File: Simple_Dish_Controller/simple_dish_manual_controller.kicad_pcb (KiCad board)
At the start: 2 copper layers, 13 parts, among them J1 Screw_Terminal_01x02, J2 DA15_Socket, J3 DA15_Socket, Q1 PZT2222A, Q2 PZT2222A, Q3 PZT2222A, Q4 PZT2222A, U1 AMS1117-5.0, U4 ICM7555xP, U5 ICM7555xP

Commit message: 777 chip is now SMD
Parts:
- added J4: CRJ022-G-TH, 2-port JR45:CUI_CRJ022-G-TH, F.Cu at (97.5, 78.1)
- added J5: CRJ022-G-TH, 2-port JR45:CUI_CRJ022-G-TH, F.Cu at (50.2, 78.1)
- C1, C2: footprint GRM219R61C226ME15K:CAPC2012X100N -> Cap_SMD_22uF_0805:CAPC2012X100N
- J2, J3: value DA15_Socket -> 1-Pin Terminal Block; footprint Connector_Dsub:DSUB-15_Socket_Horizontal_P2.77x2.54mm_EdgePinOffset9.40mm -> 2-port JR45:CUI_CRJ022-G-TH
- U4: value ICM7555xP -> NE555PS; footprint Package_SO:SOIC-8_3.9x4.9mm_P1.27mm -> NE555P Osc Chip SMD:SOIC127P780X200-8N
- U5: value ICM7555xP -> NE555PS; footprint Package_DIP:DIP-8_W7.62mm -> NE555P Osc Chip SMD:SOIC127P780X200-8N
- moved C1 339.8 mm to (89.9, 93.3)
- moved U1 317.6 mm to (85.0, 104.5)
- moved C2 314.9 mm to (89.9, 96.3)
- moved J3 313.8 mm to (50.2, 54.3)
- moved R1 304.1 mm to (88.9, 98.7)
- moved J1 298.6 mm to (82.6, 95.9)
- moved U5 279.8 mm to (72.8, 62.8)
- moved Q3 277.8 mm to (72.5, 46.4)
- moved Q4 266.3 mm to (72.5, 54.7)
- moved J2 258.1 mm to (97.5, 54.3)
- moved U4 240.2 mm to (120.1, 62.8)
- moved Q2 214.8 mm to (119.8, 54.7)
- moved Q1 196.2 mm to (119.8, 46.4)
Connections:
- net Net-(Q4-B) renamed /Azimuth/Pul sig
- net Net-(U4-R) renamed /Elevation/Pulse Enable
- net Net-(U5-R) renamed /Azimuth/Pulse Enable
- Q1 pad 2: /Elevation/Pul -> /Elevation/Dir
- Q2 pad 1: Net-(Q2-B) -> /Elevation/Pul sig
- Q2 pad 2: /Elevation/Dir -> /Elevation/Pul
- U4 pad 3: Net-(Q1-B) -> /Elevation/Pul sig

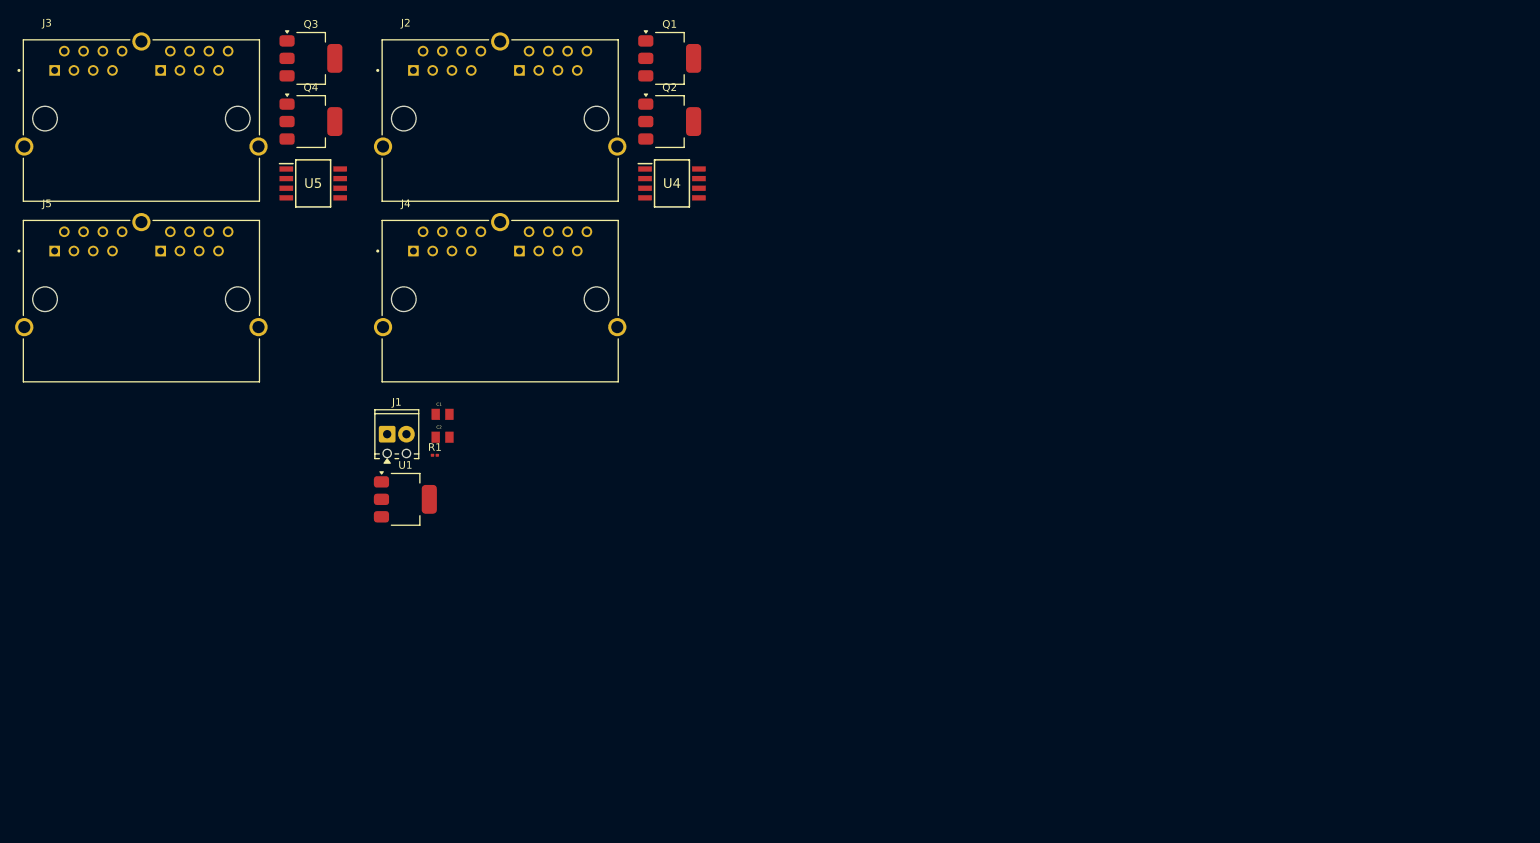
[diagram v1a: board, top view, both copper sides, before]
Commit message: Added parts dir
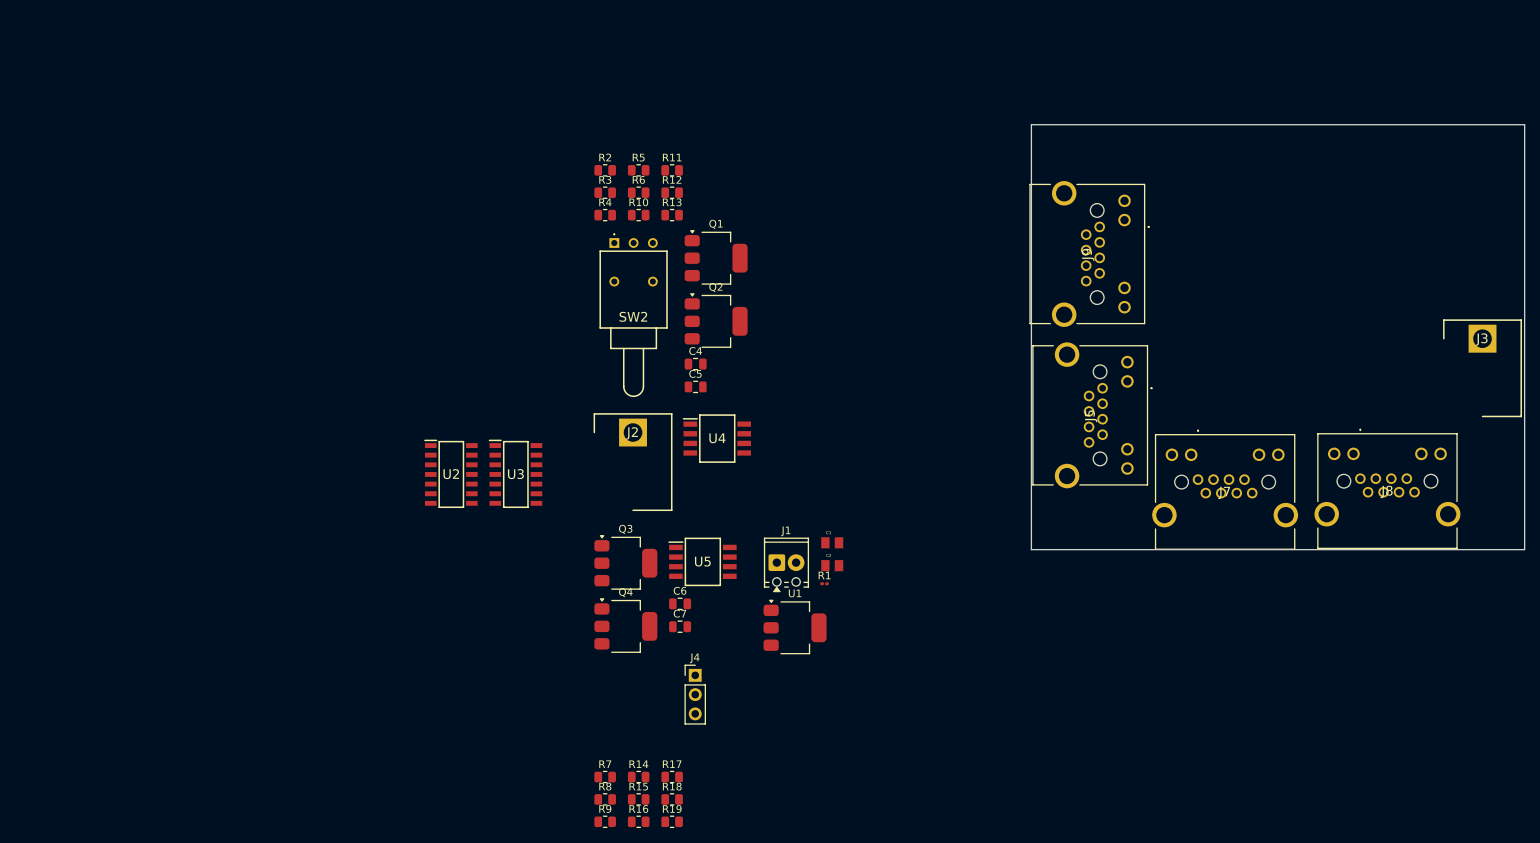
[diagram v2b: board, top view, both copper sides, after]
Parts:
- added C4: 10nF, Capacitor_SMD:C_0805_2012Metric, F.Cu at (123.2, 86.6)
- added C5: 100nF, Capacitor_SMD:C_0805_2012Metric, F.Cu at (123.2, 89.7)
- added C6: 10nF, Capacitor_SMD:C_0805_2012Metric, F.Cu at (121.2, 118.2)
- added C7: 100nF, Capacitor_SMD:C_0805_2012Metric, F.Cu at (121.2, 121.3)
- added J7: RJ45 port shielded, RA, TH, DishController_footprints:RJ45 Port Shielded, Right Angle TH, F.Cu at (189.5, 101.9)
- added J8: RJ45 port shielded, RA, TH, DishController_footprints:RJ45 Port Shielded, Right Angle TH, F.Cu at (210.8, 101.8)
- added J9: RJ45 port shielded, RA, TH, DishController_footprints:RJ45 Port Shielded, Right Angle TH, F.Cu at (176.5, 68.6)
- added R10: 10k, Resistor_SMD:R_0805_2012Metric, F.Cu at (115.7, 67.0)
- added R11: 10k, Resistor_SMD:R_0805_2012Metric, F.Cu at (120.2, 61.1)
- added R12: 10k, Resistor_SMD:R_0805_2012Metric, F.Cu at (120.2, 64.1)
- added R13: 10k, Resistor_SMD:R_0805_2012Metric, F.Cu at (120.2, 67.0)
- added R14: 10k, Resistor_SMD:R_0805_2012Metric, F.Cu at (115.7, 141.1)
- added R15: 10k, Resistor_SMD:R_0805_2012Metric, F.Cu at (115.7, 144.0)
- added R16: 10k, Resistor_SMD:R_0805_2012Metric, F.Cu at (115.7, 147.0)
- added R17: 10k, Resistor_SMD:R_0805_2012Metric, F.Cu at (120.2, 141.1)
- added R18: 820, Resistor_SMD:R_0805_2012Metric, F.Cu at (120.2, 144.0)
- added R19: 6.8k, Resistor_SMD:R_0805_2012Metric, F.Cu at (120.2, 147.0)
- added R2: 820, Resistor_SMD:R_0805_2012Metric, F.Cu at (111.3, 61.1)
- added R3: 10k, Resistor_SMD:R_0805_2012Metric, F.Cu at (111.3, 64.1)
- added R4: 6.8k, Resistor_SMD:R_0805_2012Metric, F.Cu at (111.3, 67.0)
- added R5: 10k, Resistor_SMD:R_0805_2012Metric, F.Cu at (115.7, 61.1)
- added R6: 1k, Resistor_SMD:R_0805_2012Metric, F.Cu at (115.7, 64.1)
- added R7: 10k, Resistor_SMD:R_0805_2012Metric, F.Cu at (111.3, 141.1)
- added R8: 10k, Resistor_SMD:R_0805_2012Metric, F.Cu at (111.3, 144.0)
- added R9: 1k, Resistor_SMD:R_0805_2012Metric, F.Cu at (111.3, 147.0)
- added SW2: SW_SPDT_312, SPDT-90-Deg-On-Off-On:B18JH, F.Cu at (112.5, 70.7)
- added U2: 74LS08, 74LS08_SOIC:SOIC127P600X175-14N, F.Cu at (91.1, 101.2)
- added U3: 74LS32, 74LS32_SOIC:SOIC127P600X175-14N, F.Cu at (99.6, 101.2)
- J2, J3: footprint 2-port JR45:CUI_CRJ022-G-TH -> 1-Pin Barrier Terminal Block:RHDR1W160P0X826_1X1_1020X1270X1270P
- J4: value CRJ022-G-TH -> Conn_01x03_Pin; footprint 2-port JR45:CUI_CRJ022-G-TH -> Connector_PinHeader_2.54mm:PinHeader_1x03_P2.54mm_Vertical
- J5: value CRJ022-G-TH -> RJ45 port shielded, RA, TH; footprint 2-port JR45:CUI_CRJ022-G-TH -> DishController_footprints:RJ45 Port Shielded, Right Angle TH
- moved J3 179.1 mm to (226.9, 83.3)
- moved J5 127.2 mm to (176.9, 89.8), turned to -90 degrees
- moved Q3 78.4 mm to (114.0, 112.9)
- moved Q4 78.4 mm to (114.0, 121.2)
- moved U5 71.6 mm to (124.2, 112.7)
- moved J4 55.8 mm to (123.2, 127.7)
- moved R1 54.1 mm to (140.2, 115.6)
- moved C1 54.1 mm to (141.2, 110.2)
- moved C2 54.1 mm to (141.2, 113.2)
- moved J1 54.1 mm to (133.9, 112.8)
- moved U1 54.1 mm to (136.3, 121.4)
- moved J2 44.9 mm to (115.0, 95.7)
- moved U4 34.2 mm to (126.1, 96.5)
- moved Q1 27.0 mm to (126.0, 72.7)
- moved Q2 27.0 mm to (126.0, 81.0)
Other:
- board outline added: 65 x 56 mm

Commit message: Latest update
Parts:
- removed C1, C2: 22uF, Cap_SMD_22uF_0805:CAPC2012X100N
- removed C5: 100nF, Capacitor_SMD:C_0805_2012Metric
- removed J7, J8, J9: RJ45 port shielded, RA, TH, DishController_footprints:RJ45 Port Shielded, Right Angle TH
- removed Q2: PZT2222A, Package_TO_SOT_SMD:SOT-223-3_TabPin2
- removed R2: 820, Resistor_SMD:R_0805_2012Metric
- removed R4: 6.8k, Resistor_SMD:R_0805_2012Metric
- removed SW2: SW_SPDT_312, SPDT-90-Deg-On-Off-On:B18JH
- added C3: 100nF, DishFootprints:C_0805, F.Cu at (107.6, 85.9)
- added J10: Screw Terminal 4 pins to board, DishFootprintsSupplier:TERM_SCREW_01x04_VERTICAL_KEYSTONE_7690, F.Cu at (185.5, 104.5)
- added J6: Conn_01x03_Pin, DishFootprints:PinHeader_1x03_P2.54mm_Vertical, F.Cu at (169.8, 76.1)
- added Q5: PZT2222A, DishFootprints:SOT-223, F.Cu at (124.3, 90.4)
- added R20: 820, DishFootprints:R_0805, F.Cu at (140.3, 82.3)
- added R21: 6.8k, DishFootprints:R_0805, F.Cu at (140.3, 85.2)
- C4: value 10nF -> 100nF; footprint Capacitor_SMD:C_0805_2012Metric -> DishFootprints:C_0805
- C6: value 10nF -> 10uF; footprint Capacitor_SMD:C_0805_2012Metric -> DishFootprints:C_0805
- C7: value 100nF -> 10uF; footprint Capacitor_SMD:C_0805_2012Metric -> DishFootprints:C_0805
- J1: footprint TerminalBlock_Phoenix:TerminalBlock_Phoenix_MPT-0,5-2-2.54_1x02_P2.54mm_Horizontal -> DishFootprints:TerminalBlock_Phoenix_MKDS-1,5-2-5.08_1x02_P5.08mm_Horizontal
- J2: value 1-Pin Terminal Block -> Conn_01x02_Pin; footprint 1-Pin Barrier Terminal Block:RHDR1W160P0X826_1X1_1020X1270X1270P -> DishFootprints:PinHeader_1x02_P2.54mm_Vertical
- J3: value 1-Pin Terminal Block -> DE-15_VGA_FEMALE_CONN; footprint 1-Pin Barrier Terminal Block:RHDR1W160P0X826_1X1_1020X1270X1270P -> DishFootprintsSupplier:DB15_VGA_FEMALE_CONN
- J4: footprint Connector_PinHeader_2.54mm:PinHeader_1x03_P2.54mm_Vertical -> DishFootprints:PinHeader_1x03_P2.54mm_Vertical
- J5: value RJ45 port shielded, RA, TH -> DE-15_VGA_FEMALE_CONN; footprint DishController_footprints:RJ45 Port Shielded, Right Angle TH -> DishFootprintsSupplier:DB15_VGA_FEMALE_CONN
- Q1, Q3, Q4: footprint Package_TO_SOT_SMD:SOT-223-3_TabPin2 -> DishFootprints:SOT-223
- R1: footprint Resistor_SMD:R_0201_0603Metric -> DishFootprints:R_0805
- R13, R18, R19: footprint Resistor_SMD:R_0805_2012Metric -> DishFootprints:R_0805
- U1: footprint Package_TO_SOT_SMD:SOT-223-3_TabPin2 -> DishFootprints:SOT-223-3_TabPin2
- U2: footprint 74LS08_SOIC:SOIC127P600X175-14N -> DishFootprints:SOIC-14_3.9x8.7mm_P1.27mm
- U3: footprint 74LS32_SOIC:SOIC127P600X175-14N -> DishFootprints:SOIC-14_3.9x8.7mm_P1.27mm
- U4, U5: value NE555PS -> NE555D; footprint NE555P Osc Chip SMD:SOIC127P780X200-8N -> DishFootprints:SOIC-8_3.9x4.9mm_P1.27mm
- moved U3 104.2 mm to (203.1, 88.7)
- moved U2 95.4 mm to (185.5, 87.6)
- moved U4 85.4 mm to (211.3, 90.3)
- moved Q1 82.6 mm to (208.5, 74.5)
- moved J4 66.8 mm to (169.7, 79.7), turned to 90 degrees
- moved R17 65.4 mm to (98.5, 79.3)
- moved R19 65.4 mm to (98.5, 85.2)
- moved R7 65.4 mm to (89.7, 79.3)
- moved R9 65.4 mm to (89.7, 85.2)
- moved R14 65.4 mm to (94.1, 79.3)
- moved R16 65.4 mm to (94.1, 85.2)
- moved R18 65.4 mm to (98.5, 82.3)
- moved R8 65.4 mm to (89.7, 82.3)
- moved R15 65.4 mm to (94.1, 82.3)
- moved J2 56.1 mm to (169.7, 83.2), turned to 90 degrees
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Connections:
- C4 pad 1: Net-(U4-CONT) -> Net-(U4-THR)
- C7 pad 1: Net-(U5-THRES) -> Net-(U4-CV)
- J2 pad 1: Shield -> /IN_5VDC_SWITCH
- J3 pad 1: Shield -> +5V
- J5 pad 11: unconnected-(J5-A/K_3-Pad11) -> /Elevation/Pul
- J5 pad 12: unconnected-(J5-A/K_4-Pad12) -> /Elevation/Dir
- J5 pad 3: /Azimuth/Limit Sw1 -> /Elevation/Limit Sw1
- J5 pad 4: /Azimuth/Limit Sw2 -> /Elevation/Limit Sw2
- Q1 pad 1: Net-(Q1-B) -> /Elevation/Pul sig
- Q1 pad 2: /Elevation/Dir -> /Elevation/Pul
- R18 pad 2: Net-(U5-DISCH) -> Net-(U5-DIS)
- R19 pad 1: Net-(U5-THRES) -> Net-(U5-DIS)
- R19 pad 2: Net-(U5-DISCH) -> Net-(U5-THR)
- R6 pad 2: Net-(Q1-B) -> Net-(Q5-B)
- U4 pad 2: Net-(U4-THRES) -> Net-(U4-THR)
- U4 pad 5: Net-(U4-CONT) -> Net-(U4-CV)
- U4 pad 6: Net-(U4-THRES) -> Net-(U4-THR)
- U5 pad 2: Net-(U5-THRES) -> Net-(U5-THR)
- U5 pad 6: Net-(U5-THRES) -> Net-(U5-THR)
- U5 pad 7: Net-(U5-DISCH) -> Net-(U5-DIS)

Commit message: Updates
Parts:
- removed J10: Screw Terminal 4 pins to board, DishFootprintsSupplier:TERM_SCREW_01x04_VERTICAL_KEYSTONE_7690
- removed Q5: PZT2222A, DishFootprints:SOT-223
- removed R20: 820, DishFootprints:R_0805
- removed R21: 6.8k, DishFootprints:R_0805
- added C1: 22uF, Capacitor_SMD:C_1206_3216Metric, F.Cu at (127.6, 72.3)
- added C10: 10uF, Capacitor_SMD:C_1206_3216Metric, F.Cu at (138.2, 132.5)
- added C2: 22uF, Capacitor_SMD:C_1206_3216Metric, F.Cu at (127.6, 75.7)
- added C5: 0.1uF, Capacitor_SMD:C_1206_3216Metric, F.Cu at (250.3, 78.2)
- added C8: 0.1uF, Capacitor_SMD:C_1206_3216Metric, F.Cu at (138.2, 125.8)
- added C9: 100nF, Capacitor_SMD:C_1206_3216Metric, F.Cu at (138.2, 129.1)
- added D1: LED, LED_SMD:LED_1206_3216Metric, F.Cu at (137.8, 84.4)
- added J7: Azimuth DE-15, DishFootprints:DE15_VGA_FEMALE_CONN, F.Cu at (187.4, 110.4)
- added Q2: MMBT2222A, Package_TO_SOT_SMD:SOT-23, F.Cu at (260.2, 83.5)
- added R2: 820, Resistor_SMD:R_1206_3216Metric, F.Cu at (244.7, 53.9)
- added R4: 10k, Resistor_SMD:R_1206_3216Metric, F.Cu at (244.7, 60.6)
- added REF**: Raspberry_Pi_HAT_Side_DE15_Outline, DishFootprints:Raspberry_Pi_HAT_Side_DE15_Outline, F.Cu at (170.8, 50.1)
- C3, C4: value 100nF -> 0.1uF; footprint DishFootprints:C_0805 -> Capacitor_SMD:C_1206_3216Metric
- C6: value 10uF -> 100nF; footprint DishFootprints:C_0805 -> Capacitor_SMD:C_1206_3216Metric
- C7: footprint DishFootprints:C_0805 -> Capacitor_SMD:C_1206_3216Metric
- J1: footprint DishFootprints:TerminalBlock_Phoenix_MKDS-1,5-2-5.08_1x02_P5.08mm_Horizontal -> TerminalBlock_Phoenix:TerminalBlock_Phoenix_MKDS-1,5-2-5.08_1x02_P5.08mm_Horizontal
- J2: footprint DishFootprints:PinHeader_1x02_P2.54mm_Vertical -> Connector_PinHeader_2.54mm:PinHeader_1x02_P2.54mm_Vertical
- J3: value DE-15_VGA_FEMALE_CONN -> Screw Terminal To Chassis; footprint DishFootprintsSupplier:DB15_VGA_FEMALE_CONN -> DishFootprints:TERM_SCREW_01x04_VERTICAL_KEYSTONE_7690
- J4, J6: footprint DishFootprints:PinHeader_1x03_P2.54mm_Vertical -> Connector_PinHeader_2.54mm:PinHeader_1x03_P2.54mm_Vertical
- J5: value DE-15_VGA_FEMALE_CONN -> Elevation DE-15; footprint DishFootprintsSupplier:DB15_VGA_FEMALE_CONN -> DishFootprints:DE15_VGA_FEMALE_CONN
- Q1, Q3, Q4: value PZT2222A -> MMBT2222A; footprint DishFootprints:SOT-223 -> Package_TO_SOT_SMD:SOT-23
- R1: value 1k5 -> 1k; footprint DishFootprints:R_0805 -> Resistor_SMD:R_0805_2012Metric
- R10: value 10k -> 1k; footprint Resistor_SMD:R_0805_2012Metric -> Resistor_SMD:R_1206_3216Metric
- R11: value 10k -> 820; footprint Resistor_SMD:R_0805_2012Metric -> Resistor_SMD:R_1206_3216Metric
- R12, R15, R16, R17, R3, R7, R8: footprint Resistor_SMD:R_0805_2012Metric -> Resistor_SMD:R_1206_3216Metric
- R13: footprint DishFootprints:R_0805 -> Resistor_SMD:R_1206_3216Metric
- R14, R5: value 10k -> 6.8k; footprint Resistor_SMD:R_0805_2012Metric -> Resistor_SMD:R_1206_3216Metric
- R18: value 820 -> 10k; footprint DishFootprints:R_0805 -> Resistor_SMD:R_1206_3216Metric
- R19: value 6.8k -> 1k; footprint DishFootprints:R_0805 -> Resistor_SMD:R_1206_3216Metric
- R6, R9: value 1k -> 10k; footprint Resistor_SMD:R_0805_2012Metric -> Resistor_SMD:R_1206_3216Metric
- U1: footprint DishFootprints:SOT-223-3_TabPin2 -> Package_TO_SOT_SMD:SOT-223-3_TabPin2
- U2: value 74LS08 -> 74LS32; footprint DishFootprints:SOIC-14_3.9x8.7mm_P1.27mm -> Package_SO:SOIC-14_3.9x8.7mm_P1.27mm
- U3: value 74LS32 -> 74LS08; footprint DishFootprints:SOIC-14_3.9x8.7mm_P1.27mm -> Package_SO:SOIC-14_3.9x8.7mm_P1.27mm
- U4, U5: footprint DishFootprints:SOIC-8_3.9x4.9mm_P1.27mm -> Package_SO:SOIC-8_3.9x4.9mm_P1.27mm
- moved R7 155.2 mm to (244.7, 70.5)
- moved R8 155.2 mm to (244.7, 73.8)
- moved R9 155.2 mm to (244.7, 77.1)
- moved C6 142.9 mm to (250.3, 81.5)
- moved R3 115.3 mm to (244.7, 57.3)
- moved R5 114.7 mm to (244.7, 63.9)
- moved R6 114.6 mm to (244.7, 67.2)
- moved R10 108.8 mm to (244.7, 80.4)
- moved C7 101.0 mm to (250.3, 84.9)
- moved J4 85.7 mm to (255.4, 78.8), turned to 0 degrees
- moved Q3 79.1 mm to (148.1, 126.5)
- moved Q4 77.1 mm to (148.1, 131.1)
- moved U3 69.6 mm to (137.4, 65.6)
- moved U5 64.6 mm to (154.7, 127.4)
- moved U2 60.6 mm to (129.0, 65.6)
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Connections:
- C3 pad 1: Net-(U5-THR) -> +5V
- C4 pad 1: Net-(U4-THR) -> +5V
- C6 pad 1: Net-(U5-CV) -> Net-(U4-THR)
- J4 pad 1: /Azimuth/Dir Sig -> /Elevation/Dir Sig
- J4 pad 3: Net-(J4-Pad3) -> Net-(J4-Pin_3)
- J6 pad 1: /Elevation/Dir Sig -> /Azimuth/Dir Sig
- J6 pad 3: Net-(J6-Pad3) -> Net-(J6-Pin_3)
- Q1 pad 1: /Elevation/Pul sig -> Net-(Q1-B)
- Q1 pad 2: /Elevation/Pul -> GND
- Q1 pad 3: GND -> /Elevation/Dir
- Q3 pad 2: /Azimuth/Dir -> GND
- Q3 pad 3: GND -> /Azimuth/Dir
- Q4 pad 2: /Azimuth/Pul -> GND
- Q4 pad 3: GND -> /Azimuth/Pul
- R10 pad 1: /Elevation/Limit Sw2 -> /Elevation/Dir Sig
- R10 pad 2: GND -> Net-(Q1-B)
- R11 pad 1: /Elevation/Limit Sw1 -> Net-(U5-DIS)
- R11 pad 2: GND -> +5V
- R12 pad 1: Net-(R12-Pad1) -> /Azimuth/Dir Sig
- R13 pad 1: Net-(R13-Pad1) -> /Azimuth/Limit Sw1
- R14 pad 1: /Azimuth/Limit Sw1 -> Net-(U5-THR)
- R14 pad 2: GND -> Net-(U5-DIS)
- R15 pad 1: Net-(J4-Pad3) -> Net-(R15-Pad1)
- R17 pad 1: Net-(R17-Pad1) -> Net-(J6-Pin_3)
- R18 pad 1: +5V -> Net-(J6-Pin_3)
- R18 pad 2: Net-(U5-DIS) -> GND
- R19 pad 1: Net-(U5-DIS) -> /Azimuth/Dir Sig
- R19 pad 2: Net-(U5-THR) -> Net-(Q3-B)
- R5 pad 1: Net-(J6-Pad3) -> Net-(U4-THR)
- R5 pad 2: GND -> Net-(U4-DIS)
- R6 pad 1: /Elevation/Dir Sig -> Net-(R6-Pad1)
- R6 pad 2: Net-(Q5-B) -> GND
- R7 pad 1: /Azimuth/Dir Sig -> Net-(R7-Pad1)
- R8 pad 1: Net-(J4-Pad3) -> Net-(J4-Pin_3)
- R9 pad 1: /Azimuth/Dir Sig -> /Elevation/Limit Sw2
- R9 pad 2: Net-(Q3-B) -> GND
- U2 pad 1: /Elevation/Limit Sw1 -> Net-(R6-Pad1)
- U2 pad 10: /Azimuth/Dir Sig -> unconnected-(U2-Pad10)
- U2 pad 11: Net-(R17-Pad1) -> unconnected-(U2-Pad11)
- U2 pad 12: /Azimuth/Limit Sw2 -> unconnected-(U2-Pad12)
- U2 pad 13: Net-(J4-Pad3) -> unconnected-(U2-Pad13)
- U2 pad 2: /Elevation/Dir Sig -> Net-(R7-Pad1)
- U2 pad 3: Net-(R12-Pad1) -> /Elevation/Pulse Enable
- U2 pad 4: /Elevation/Limit Sw2 -> Net-(R15-Pad1)
- U2 pad 5: Net-(J6-Pad3) -> Net-(R16-Pad1)
- U2 pad 6: Net-(R13-Pad1) -> /Azimuth/Pulse Enable
- U2 pad 8: Net-(R16-Pad1) -> unconnected-(U2-Pad8)
- U2 pad 9: /Azimuth/Limit Sw1 -> unconnected-(U2-Pad9)
- U3 pad 1: Net-(R12-Pad1) -> /Elevation/Limit Sw1
- U3 pad 10: unconnected-(U3-Pad10) -> /Azimuth/Dir Sig
- U3 pad 11: unconnected-(U3-Pad11) -> Net-(R16-Pad1)
- U3 pad 12: unconnected-(U3-Pad12) -> /Azimuth/Limit Sw2
- U3 pad 13: unconnected-(U3-Pad13) -> Net-(J6-Pin_3)
- U3 pad 2: Net-(R13-Pad1) -> /Elevation/Dir Sig
- U3 pad 3: /Elevation/Pulse Enable -> Net-(R6-Pad1)
- U3 pad 4: Net-(R16-Pad1) -> /Elevation/Limit Sw2
- U3 pad 5: Net-(R17-Pad1) -> Net-(J4-Pin_3)
- U3 pad 6: /Azimuth/Pulse Enable -> Net-(R7-Pad1)
- U3 pad 8: unconnected-(U3-Pad8) -> Net-(R15-Pad1)
- U3 pad 9: unconnected-(U3-Pad9) -> /Azimuth/Limit Sw1
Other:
- board size 65 x 56 mm -> 65 x 75 mm
- copper layers 2 -> 4

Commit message: minor update to PCB
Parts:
- removed REF**: Raspberry_Pi_HAT_Side_DE15_Outline, DishFootprints:Raspberry_Pi_HAT_Side_DE15_Outline
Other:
- board outline removed
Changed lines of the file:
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@@
 		)
-	)
-	(footprint "DishFootprints:Raspberry_Pi_HAT_Side_DE15_Outline"
-		(layer "F.Cu")
-		(at 170.8 50.1)
-		(descr "Raspberry Pi HAT standard outline with mounting holes")
-		(tags "Raspberry Pi HAT")
-		(property "Reference" "REF**"
-			(at 0 0 0)
-			(layer "F.SilkS")
-			(hide yes)
-			(effects
-				(font
-					(size 1 1)
-					(thickness 0.15)
-				)
-			)
-		)
-		(property "Value" "Raspberry_Pi_HAT_Side_DE15_Outline"
-			(at 0 -5 0)
-			(layer "F.Fab")
-			(effects
-				(font
-					(size 1 1)
-					(thickness 0.15)
-				)
-			)
-		)
-		(property "Datasheet" ""
-			(at 0 0 0)
-			(layer "F.Fab")
-			(hide yes)
-			(effects
-				(font
-					(size 1.27 1.27)
-					(thickness 0.15)
-				)
-			)
-		)
-		(property "Description" "Raspberry Pi HAT outline with holes"
-			(at 0 0 0)
-			(layer "F.Fab")
-			(hide yes)
-			(effects
-				(font
-					(size 1.27 1.27)
-					(thickness 0.15)
-				)
-			)
-		)
-		(property "Note" "From a ChatGPT discussion"
-			(at 0 0 0)
-			(layer "F.SilkS")
-			(effects
-				(font
-					(size 1 1)
-					(thickness 0.1)
-				)
-			)
-		)
-		(attr exclude_from_pos_files exclude_from_bom)
-		(fp_line
-			(start 0 0)
-			(end 65 0)
-			(stroke
-				(width 0.05)
-				(type solid)
-			)
-			(layer "Edge.Cuts")
-		)
-		(fp_line
-			(start 0 75)
-			(end 0 0)
-			(stroke
-				(width 0.05)
-				(type solid)
-			)
-			(layer "Edge.Cuts")
-		)
-		(fp_line
-			(start 65 0)
-			(end 65 75)
-			(stroke
-				(width 0.05)
-				(type solid)
-			)
-			(layer "Edge.Cuts")
-		)
-		(fp_line
-			(start 65 75)
-			(end 0 75)
-			(stroke
-				(width 0.05)
-				(type solid)
-			)
-			(layer "Edge.Cuts")
-		)
-		(pad "" np_thru_hole circle
-			(at 2.5 2.5)
-			(size 2.75 2.75)
-			(drill 2.75)
-			(layers "*.Mask")
-		)
-		(pad "" np_thru_hole circle
-			(at 2.5 53.5)
-			(size 2.75 2.75)
-			(drill 2.75)
-			(layers "*.Mask")
-		)
-		(pad "" np_thru_hole circle
-			(at 62.5 2.5)
-			(size 2.75 2.75)
-			(drill 2.75)
-			(layers "*.Mask")
-		)
-		(pad "" np_thru_hole circle
-			(at 62.5 53.5)
-			(size 2.75 2.75)
-			(drill 2.75)
-			(layers "*.Mask")
-		)
-		(embedded_fonts no)
 	)
 	(footprint "Resistor_SMD:R_1206_3216Metric"
